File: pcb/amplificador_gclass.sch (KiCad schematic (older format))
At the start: 51 parts, among them J1 Jack_3.5mm_5pin, P1 CONN_01X01, P10 CONN_01X01, P12 OUT, P13 CONN_01X01, P2 CONN_01X01, P3 CONN_01X01, P4 CONN_01X01, P5 CONN_01X01, P6 CONN_01X01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

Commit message: algun cambio
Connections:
- net +VA: no longer R13.1
- net at Q6.2 (B), R13.2: now also Q4.1 (E)
- net at Q9.2 (B), R32.2: now also Q11.1 (E)
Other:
- moved on the sheet: R13
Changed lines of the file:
@@
 L R R13
 U 1 1 558772BE
-P 4350 1750
-F 0 "R13" V 4430 1750 50  0000 C CNN
-F 1 "R" V 4350 1750 50  0000 C CNN
-F 2 "Resistors_ThroughHole:Resistor_Horizontal_RM10mm" V 4280 1750 30  0001 C CNN
-F 3 "" H 4350 1750 30  0000 C CNN
-	1    4350 1750
+P 4350 1700
+F 0 "R13" V 4430 1700 50  0000 C CNN
+F 1 "R" V 4350 1700 50  0000 C CNN
+F 2 "Resistors_ThroughHole:Resistor_Horizontal_RM10mm" V 4280 1700 30  0001 C CNN
+F 3 "" H 4350 1700 30  0000 C CNN
+	1    4350 1700
 	1    0    0    -1
 $EndComp
 Wire Wire Line
-	4350 1850 4350 2050
-Wire Wire Line
 	4350 1600 4350 1500
-Wire Wire Line
-	4350 1900 4900 1900
 Wire Wire Line
 	4650 2250 5200 2250
@@
 $EndComp
 Wire Wire Line
-	8400 1850 8400 2050
-Wire Wire Line
 	8400 1600 8400 1500
-Wire Wire Line
-	8400 1900 7850 1900
 Wire Wire Line
 	8100 2250 7550 2250
@@
 	0    -1   -1   0
 $EndComp
+Wire Wire Line
+	4350 1850 4350 2050
+Wire Wire Line
+	4900 1900 4350 1900
+Connection ~ 4350 1900
+Wire Wire Line
+	8400 1900 8400 2050
+Wire Wire Line
+	7850 1900 8150 1900
+Wire Wire Line
+	8150 1900 8150 1950
+Wire Wire Line
+	8150 1950 8400 1950
+Connection ~ 8400 1950
 $EndSCHEMATC

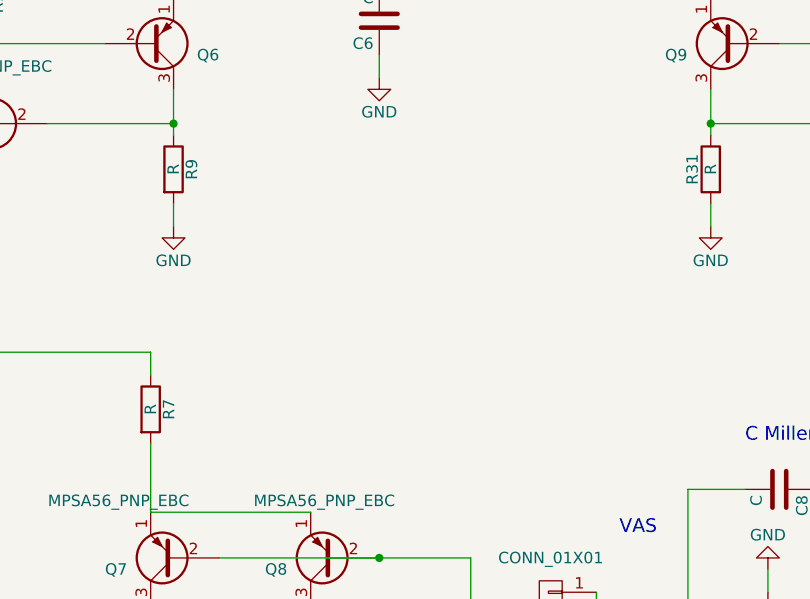
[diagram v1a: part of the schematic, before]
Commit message: Trabajando con THS4532
Agrego Footprint y model hecho a mano del THS.
Agrego modelo Spice THS (ver si funca).
Agrego el informe main.pdf asi Fede lo puede ver.
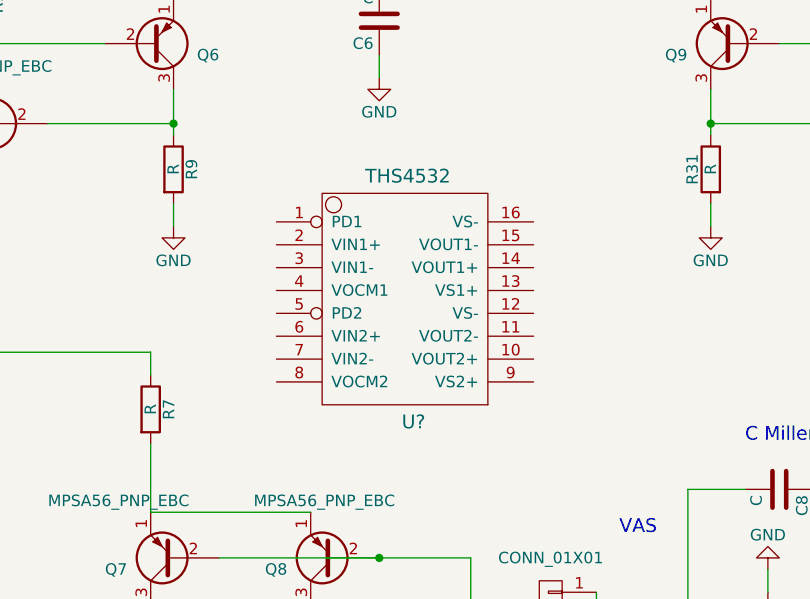
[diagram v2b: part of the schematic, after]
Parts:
- added U?: THS4532, symbol THS4532
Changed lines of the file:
@@
 	8150 1950 8400 1950
 Connection ~ 8400 1950
+$Comp
+L THS4532 U?
+U 1 1 565BC6B9
+P 6200 2980
+F 0 "U?" H 6250 2405 60  0000 C CNN
+F 1 "THS4532" H 6225 3480 60  0000 C CNN
+F 2 "" H 6225 2330 60  0000 C CNN
+F 3 "" H 6225 2330 60  0000 C CNN
+	1    6200 2980
+	1    0    0    -1
+$EndComp
 $EndSCHEMATC

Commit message: Limpio, agrego cosas
Agrego carpeta aparte para ampli usando THS.
Agrego datasheet de THS4532.
Odeno capeta simulaciones.
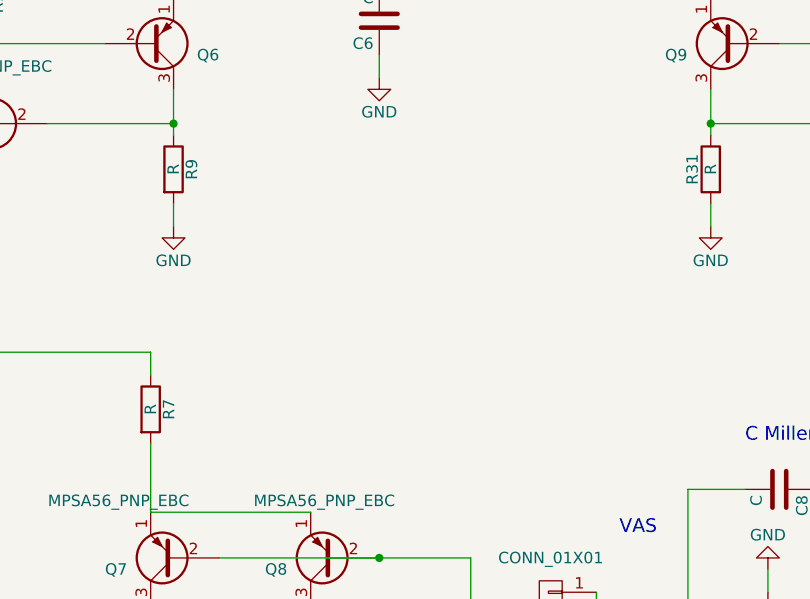
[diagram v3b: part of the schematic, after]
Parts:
- removed U?: THS4532, symbol THS4532
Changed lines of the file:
@@
 	8150 1950 8400 1950
 Connection ~ 8400 1950
-$Comp
-L THS4532 U?
-U 1 1 565BC6B9
-P 6200 2980
-F 0 "U?" H 6250 2405 60  0000 C CNN
-F 1 "THS4532" H 6225 3480 60  0000 C CNN
-F 2 "" H 6225 2330 60  0000 C CNN
-F 3 "" H 6225 2330 60  0000 C CNN
-	1    6200 2980
-	1    0    0    -1
-$EndComp
 $EndSCHEMATC
